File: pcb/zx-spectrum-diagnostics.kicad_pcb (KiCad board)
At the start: 2 copper layers, 99.9 x 98.2 mm, 75 parts, among them J101 Conn_01x04, J201 Conn_01x20_Female, J202 Conn_01x20_Female, J203 Conn_01x20_Female, Q101 PMBT2222A, SW101 SW_SPST, SW102 SW_SPST, U101 Pico, U102 Pico

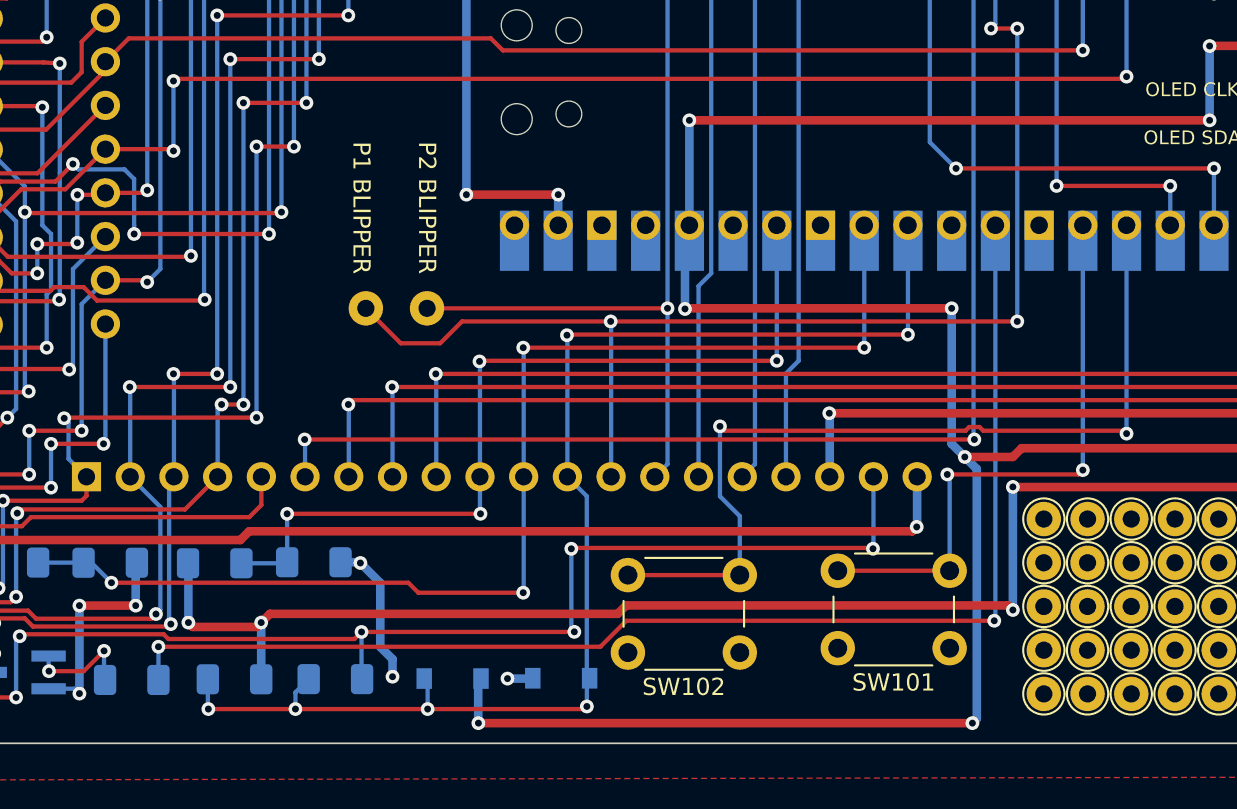
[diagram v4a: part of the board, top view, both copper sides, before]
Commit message: remove button2, reuse GPIO for ZXIORQ
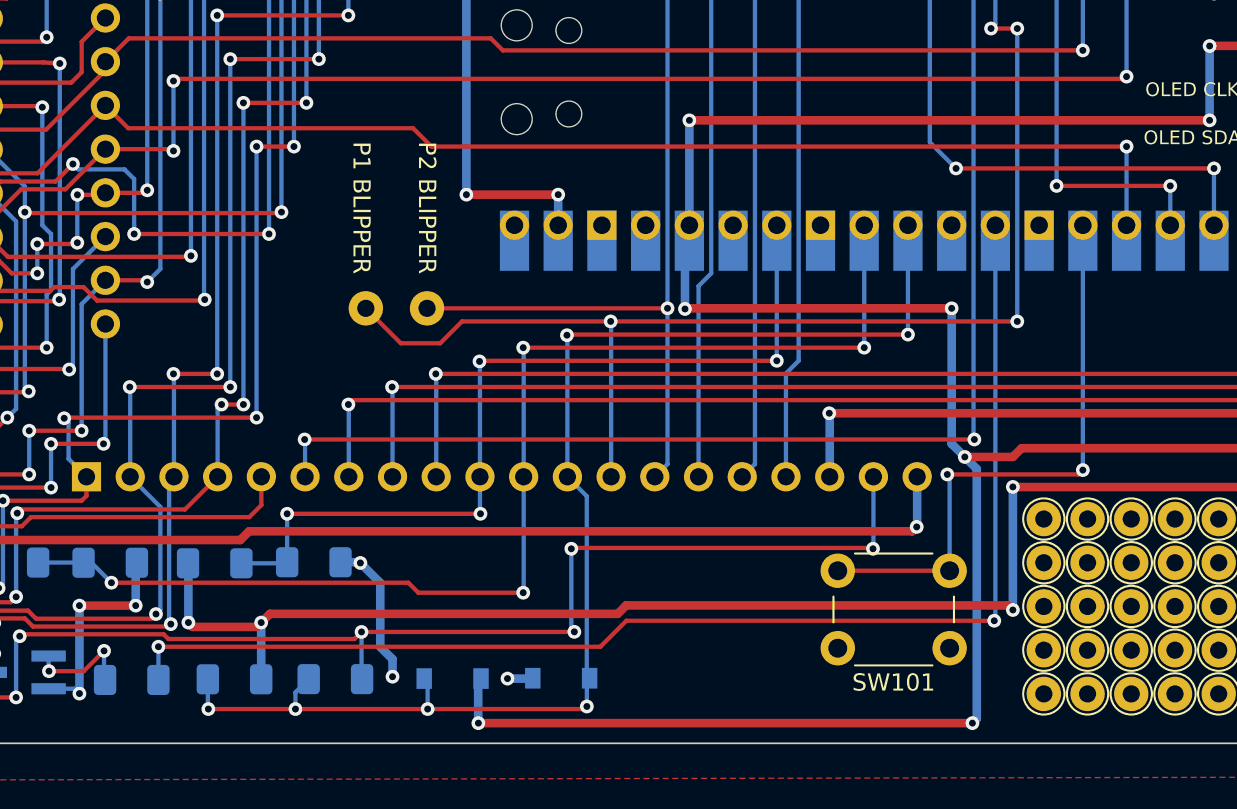
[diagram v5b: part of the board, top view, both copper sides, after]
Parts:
- removed SW102: SW_SPST, Button_Switch_THT:SW_PUSH_6mm_H4.3mm
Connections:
- U101 pad 26: INPUT2 -> ZXIORQ
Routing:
- net ZXIORQ: track 13.5 -> 78.4 mm, vias 0 -> 1
- net INPUT2: track 51.7 -> 0.00 mm, vias 2 -> 0
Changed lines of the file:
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@@
   (net 83 "PICO_RESET_Z80")
   (net 84 "INPUT1")
-  (net 85 "INPUT2")
-  (net 86 "unconnected-(Z101-PadA4)")
-  (net 87 "unconnected-(Z101-PadA28)")
+  (net 85 "unconnected-(Z101-PadA4)")
+  (net 86 "unconnected-(Z101-PadA28)")
   (footprint "TestPoint:TestPoint_THTPad_D2.0mm_Drill1.0mm" (layer "F.Cu")
     (at 166.69 148.64)
@@
       (net 61 "ZXD7") (pinfunction "D7") (pintype "input"))
     (pad "A4" thru_hole oval locked (at -25.4 -2.54 270) (size 1.7272 2.8) (drill 1.2) (layers *.Cu *.Mask)
-      (net 86 "unconnected-(Z101-PadA4)") (pinfunction "NC") (pintype "input+no_connect"))
+      (net 85 "unconnected-(Z101-PadA4)") (pinfunction "NC") (pintype "input+no_connect"))
     (pad "A6" thru_hole oval locked (at -20.32 -2.54 270) (size 1.7272 2.8) (drill 1.2) (layers *.Cu *.Mask)
       (net 62 "ZXD0") (pinfunction "D0") (pintype "input"))
@@
       (net 70 "ZXA10") (pinfunction "A10") (pintype "input"))
     (pad "A28" thru_hole oval locked (at 35.56 -2.54 270) (size 1.7272 2.8) (drill 1.2) (layers *.Cu *.Mask)
-      (net 87 "unconnected-(Z101-PadA28)") (pinfunction "NC") (pintype "input+no_connect"))
+      (net 86 "unconnected-(Z101-PadA28)") (pinfunction "NC") (pintype "input+no_connect"))
     (pad "B1" thru_hole oval locked (at -33.02 2.54 270) (size 1.7272 2.8) (drill 1.2) (layers *.Cu *.Mask)
       (net 58 "ZXA14") (pinfunction "A14") (pintype "input"))
@@
     (pad "1" thru_hole circle (at 0 0) (size 2 2) (drill 1) (layers *.Cu *.Mask))
   )
-  (footprint "Button_Switch_THT:SW_PUSH_6mm_H4.3mm" (layer "F.Cu")
-    (at 130.946 148.778 180)
-    (descr "tactile push button, 6x6mm e.g. PHAP33xx series, height=4.3mm")
-    (tags "tact sw push 6mm")
-    (property "Sheetfile" "zx-spectrum-diagnostics.kicad_sch")
-    (property "Sheetname" "")
-    (attr through_hole)
-    (fp_text reference "SW102" (at 3.25 -2) (layer "F.SilkS")
-      (effects (font (size 1 1) (thickness 0.15)))
-    )
-    (fp_text value "SW_SPST" (at 3.75 6.7) (layer "F.Fab")
-      (effects (font (size 1 1) (thickness 0.15)))
-    )
-    (fp_text user "${REFERENCE}" (at 3.25 2.25) (layer "F.Fab")
-      (effects (font (size 1 1) (thickness 0.15)))
-    )
-    (fp_line (start 5.5 -1) (end 1 -1) (layer "F.SilkS") (width 0.12))
-    (fp_line (start -0.25 1.5) (end -0.25 3) (layer "F.SilkS") (width 0.12))
-    (fp_line (start 1 5.5) (end 5.5 5.5) (layer "F.SilkS") (width 0.12))
-    (fp_line (start 6.75 3) (end 6.75 1.5) (layer "F.SilkS") (width 0.12))
-    (fp_line (start -1.5 5.75) (end -1.5 6) (layer "F.CrtYd") (width 0.05))
-    (fp_line (start 8 -1.25) (end 8 5.75) (layer "F.CrtYd") (width 0.05))
-    (fp_line (start -1.5 -1.25) (end -1.5 -1.5) (layer "F.CrtYd") (width 0.05))
-    (fp_line (start -1.5 6) (end -1.25 6) (layer "F.CrtYd") (width 0.05))
-    (fp_line (start 7.75 6) (end 8 6) (layer "F.CrtYd") (width 0.05))
-    (fp_line (start -1.5 -1.5) (end -1.25 -1.5) (layer "F.CrtYd") (width 0.05))
-    (fp_line (start 7.75 6) (end -1.25 6) (layer "F.CrtYd") (width 0.05))
-    (fp_line (start 8 -1.5) (end 8 -1.25) (layer "F.CrtYd") (width 0.05))
-    (fp_line (start 8 6) (end 8 5.75) (layer "F.CrtYd") (width 0.05))
-    (fp_line (start -1.5 5.75) (end -1.5 -1.25) (layer "F.CrtYd") (width 0.05))
-    (fp_line (start -1.25 -1.5) (end 7.75 -1.5) (layer "F.CrtYd") (width 0.05))
-    (fp_line (start 7.75 -1.5) (end 8 -1.5) (layer "F.CrtYd") (width 0.05))
-    (fp_line (start 6.25 5.25) (end 0.25 5.25) (layer "F.Fab") (width 0.1))
-    (fp_line (start 0.25 -0.75) (end 3.25 -0.75) (layer "F.Fab") (width 0.1))
-    (fp_line (start 0.25 5.25) (end 0.25 -0.75) (layer "F.Fab") (width 0.1))
-    (fp_line (start 3.25 -0.75) (end 6.25 -0.75) (layer "F.Fab") (width 0.1))
-    (fp_line (start 6.25 -0.75) (end 6.25 5.25) (layer "F.Fab") (width 0.1))
-    (fp_circle (center 3.25 2.25) (end 1.25 2.5) (layer "F.Fab") (width 0.1) (fill none))
-    (pad "1" thru_hole circle (at 0 0 270) (size 2 2) (drill 1.1) (layers *.Cu *.Mask)
-      (net 5 "GND") (pinfunction "A") (pintype "passive"))
-    (pad "1" thru_hole circle (at 6.5 0 270) (size 2 2) (drill 1.1) (layers *.Cu *.Mask)
-      (net 5 "GND") (pinfunction "A") (pintype "passive"))
-    (pad "2" thru_hole circle (at 0 4.5 270) (size 2 2) (drill 1.1) (layers *.Cu *.Mask)
-      (net 85 "INPUT2") (pinfunction "B") (pintype "passive"))
-    (pad "2" thru_hole circle (at 6.5 4.5 270) (size 2 2) (drill 1.1) (layers *.Cu *.Mask)
-      (net 85 "INPUT2") (pinfunction "B") (pintype "passive"))
-    (model "${KICAD6_3DMODEL_DIR}/Button_Switch_THT.3dshapes/SW_PUSH_6mm_H4.3mm.wrl"
-      (offset (xyz 0 0 0))
-      (scale (xyz 1 1 1))
-      (rotate (xyz 0 0 0))
-    )
-  )
   (footprint "TestPoint:TestPoint_THTPad_D2.0mm_Drill1.0mm" (layer "F.Cu")
     (at 164.15 141.02)
@@
       (net 13 "P2_LINKIN") (pinfunction "GPIO19") (pintype "bidirectional"))
     (pad "26" thru_hole oval (at 8.89 -11.43 270) (size 1.7 1.7) (drill 1.02) (layers *.Cu *.Mask)
-      (net 85 "INPUT2") (pinfunction "GPIO20") (pintype "bidirectional"))
+      (net 78 "ZXIORQ") (pinfunction "GPIO20") (pintype "bidirectional"))
     (pad "26" smd rect (at 8.89 -11.43 270) (size 3.5 1.7) (drill (offset 0.9 0)) (layers "B.Cu" "B.Mask")
-      (net 85 "INPUT2") (pinfunction "GPIO20") (pintype "bidirectional"))
+      (net 78 "ZXIORQ") (pinfunction "GPIO20") (pintype "bidirectional"))
     (pad "27" thru_hole oval (at 8.89 -8.89 270) (size 1.7 1.7) (drill 1.02) (layers *.Cu *.Mask)
       (net 84 "INPUT1") (pinfunction "GPIO21") (pintype "bidirectional"))
@@
   (gr_line (start 141.158 150.338) (end 141.92 149.576) (layer "B.SilkS") (width 0.15))
   (gr_rect (start 143.088 136.981) (end 135.128 140.462) (layer "B.SilkS") (width 0.15) (fill solid))
-  (gr_line (start 128.966 150.338) (end 129.728 149.83) (layer "B.SilkS") (width 0.15))
-  (gr_line (start 126.426 150.592) (end 125.664 149.83) (layer "B.SilkS") (width 0.15))
   (gr_line (start 138.872 150.338) (end 137.856 149.576) (layer "B.SilkS") (width 0.15))
   (gr_rect (start 76.2 90.678) (end 84.396 92.68) (layer "F.SilkS") (width 0.15) (fill solid))
@@
     (effects (font (size 0.8 0.8) (thickness 0.125)) (justify right mirror))
   )
-  (gr_text "GNDs" (at 127.696 150.846) (layer "B.SilkS")
-    (effects (font (size 0.5 0.5) (thickness 0.125)) (justify mirror))
-  )
   (gr_text "P1\nBLIP" (at 123.444 141.224) (layer "B.SilkS")
     (effects (font (size 0.8 0.8) (thickness 0.125)) (justify mirror))
@@
   (segment (start 153.416 115.316) (end 153.416 106.172) (width 0.25) (layer "B.Cu") (net 77))
   (segment (start 98.044 119.634) (end 98.044 115.57) (width 0.25) (layer "B.Cu") (net 77))
+  (segment (start 113.03 119.38) (end 153.416 119.38) (width 0.25) (layer "F.Cu") (net 78))
   (segment (start 85.374 122.144) (end 82.738 122.144) (width 0.25) (layer "F.Cu") (net 78))
   (segment (start 94.09 116.99) (end 90.145 120.935) (width 0.25) (layer "F.Cu") (net 78))
+  (segment (start 111.965123 118.315123) (end 113.03 119.38) (width 0.25) (layer "F.Cu") (net 78))
   (segment (start 86.583 120.935) (end 85.374 122.144) (width 0.25) (layer "F.Cu") (net 78))
+  (segment (start 95.415123 118.315123) (end 111.965123 118.315123) (width 0.25) (layer "F.Cu") (net 78))
   (segment (start 90.145 120.935) (end 86.583 120.935) (width 0.25) (layer "F.Cu") (net 78))
+  (segment (start 94.09 116.99) (end 95.415123 118.315123) (width 0.25) (layer "F.Cu") (net 78))
+  (via (at 153.416 119.38) (size 0.8) (drill 0.4) (layers "F.Cu" "B.Cu") (net 78))
+  (segment (start 153.416 119.38) (end 153.416 123.952) (width 0.25) (layer "B.Cu") (net 78))
   (segment (start 94.09 114.952) (end 90.647 118.395) (width 0.25) (layer "F.Cu") (net 79))
   (segment (start 95.445 113.095) (end 116.481122 113.095) (width 0.25) (layer "F.Cu") (net 79))
@@
   (segment (start 143.138 138.566) (end 143.002 138.43) (width 0.25) (layer "B.Cu") (net 84))
   (segment (start 143.138 144.024) (end 143.138 138.566) (width 0.25) (layer "B.Cu") (net 84))
-  (segment (start 144.873702 135.673) (end 144.273092 135.673) (width 0.25) (layer "F.Cu") (net 85))
-  (segment (start 130.048 135.89) (end 129.794 135.636) (width 0.25) (layer "F.Cu") (net 85))
-  (segment (start 145.090702 135.89) (end 144.873702 135.673) (width 0.25) (layer "F.Cu") (net 85))
-  (segment (start 153.416 136.0565) (end 153.2495 135.89) (width 0.25) (layer "F.Cu") (net 85))
-  (segment (start 153.2495 135.89) (end 145.090702 135.89) (width 0.25) (layer "F.Cu") (net 85))
-  (segment (start 144.273092 135.673) (end 144.056092 135.89) (width 0.25) (layer "F.Cu") (net 85))
-  (segment (start 144.056092 135.89) (end 130.048 135.89) (width 0.25) (layer "F.Cu") (net 85))
-  (segment (start 124.446 144.278) (end 130.946 144.278) (width 0.25) (layer "F.Cu") (net 85))
-  (via (at 153.416 136.0565) (size 0.8) (drill 0.4) (layers "F.Cu" "B.Cu") (net 85))
-  (via (at 129.794 135.636) (size 0.8) (drill 0.4) (layers "F.Cu" "B.Cu") (net 85))
-  (segment (start 153.416 136.0565) (end 153.416 123.952) (width 0.25) (layer "B.Cu") (net 85))
-  (segment (start 130.946 140.852) (end 129.794 139.7) (width 0.25) (layer "B.Cu") (net 85))
-  (segment (start 129.794 139.7) (end 129.794 135.636) (width 0.25) (layer "B.Cu") (net 85))
-  (segment (start 130.946 144.278) (end 130.946 140.852) (width 0.25) (layer "B.Cu") (net 85))
   (zone (net 5) (net_name "GND") (layer "F.Cu") (hatch edge 0.508)
     (connect_pads (clearance 0.508))

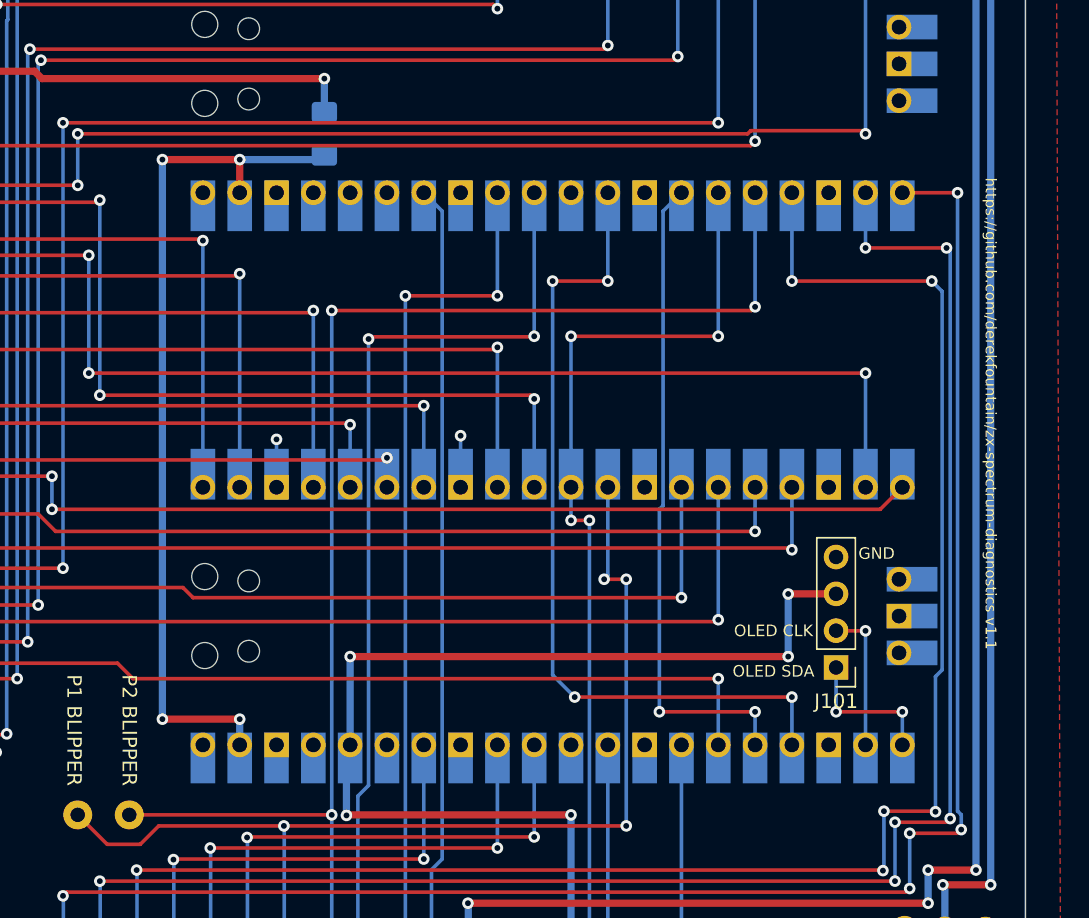
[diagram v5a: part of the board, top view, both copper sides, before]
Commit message: have a required test value sent over to pico2 at the start. add test code to fill the address buffer. works but shows the odd restarting effect i saw when i was doing the ROM emulator
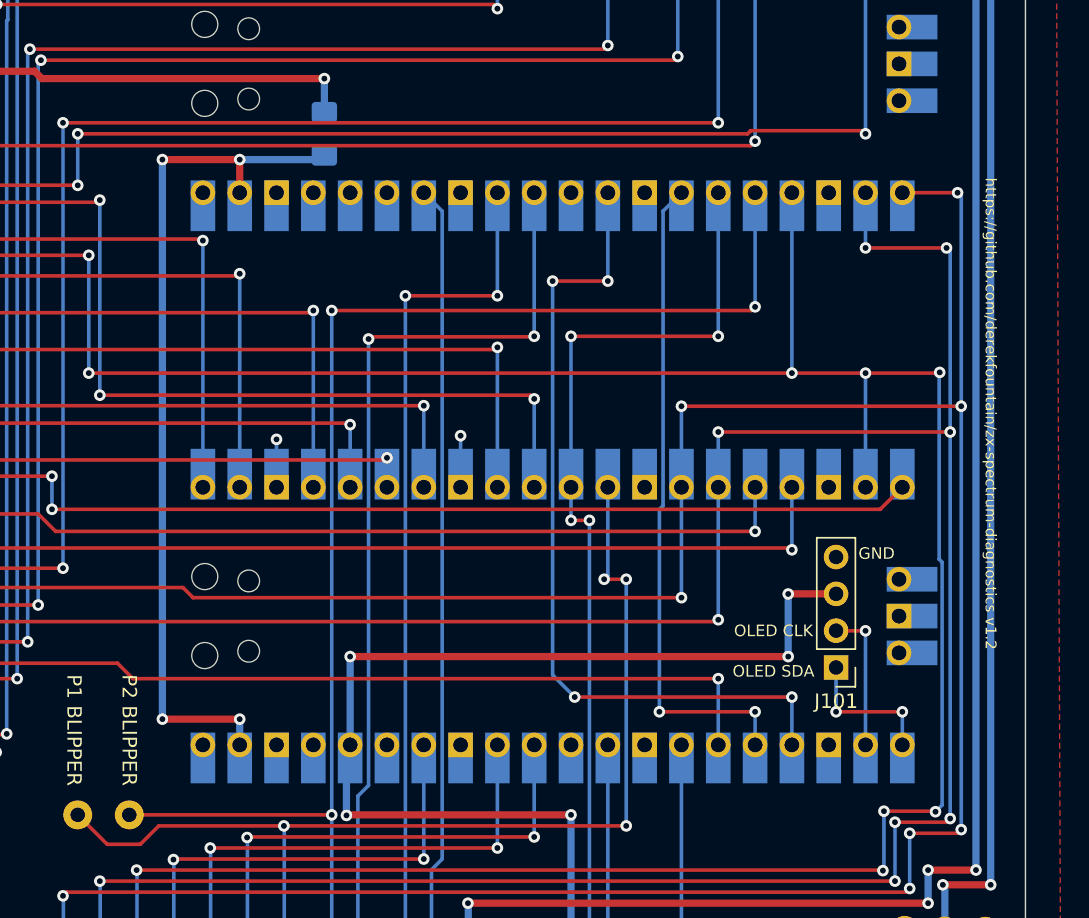
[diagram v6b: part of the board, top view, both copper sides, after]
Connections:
- J202 pad 7: P2_GPIO16 -> ZXMREQ
- J202 pad 8: P2_GPIO17 -> ZXRD
- J202 pad 9: P2_GPIO18 -> ZXCLK
- U102 pad 21: P2_GPIO16 -> ZXMREQ
- U102 pad 22: P2_GPIO17 -> ZXRD
- U102 pad 24: P2_GPIO18 -> ZXCLK
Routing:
- net ZXMREQ: track 78.6 -> 221.6 mm, vias 1 -> 8
- net ZXRD: track 86.2 -> 223.0 mm, vias 3 -> 11
- net P2_GPIO16: track 118.2 -> 0.00 mm, vias 5 -> 0
- net P2_GPIO18: track 118.0 -> 0.00 mm, vias 6 -> 0
- net P2_GPIO17: track 116.9 -> 0.00 mm, vias 6 -> 0
- net ZXCLK: track 112.5 -> 225.9 mm, vias 7 -> 13
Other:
- board text added: "https://github.com/derekfountain/zx-spectrum-diagnostics v1.2"
- board text removed: "https://github.com/derekfountain/zx-spectrum-diagnostics v1.1"

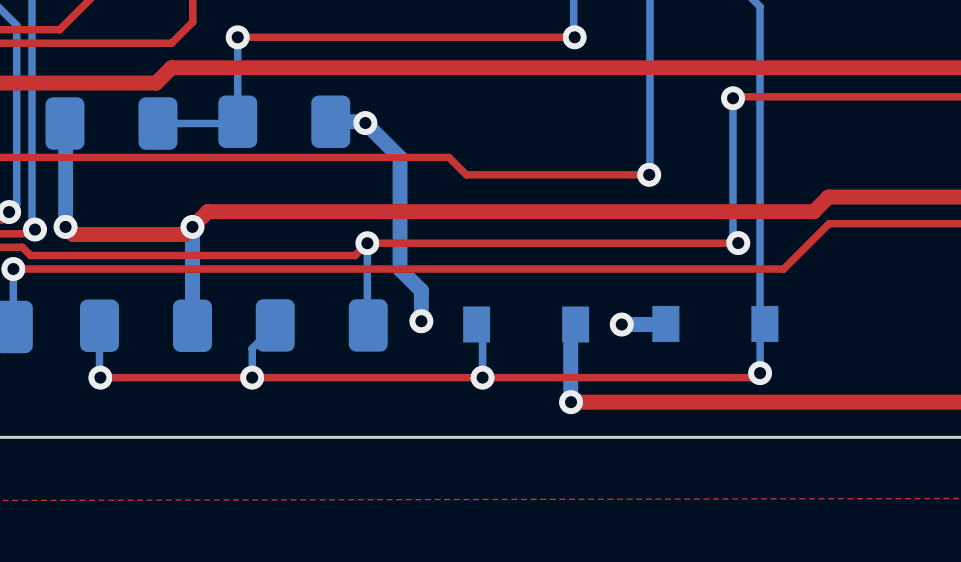
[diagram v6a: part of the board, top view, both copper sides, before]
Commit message: update schematic and PCB with revised -5V voltage divider
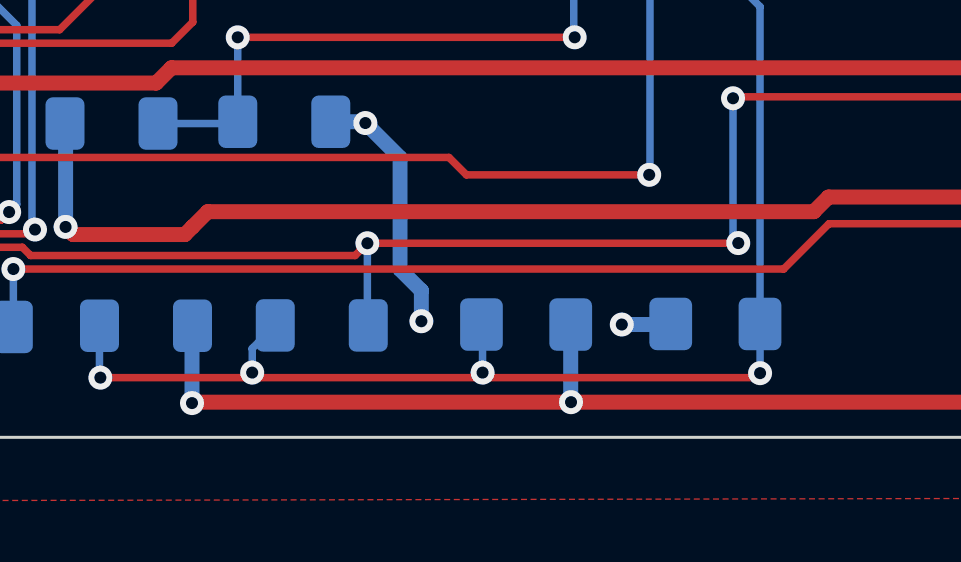
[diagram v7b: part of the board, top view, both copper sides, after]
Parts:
- D102, D103: value 1N4148 -> D_Schottky; footprint Diode_SMD:D_SOD-123 -> Diode_SMD:D_1206_3216Metric_Pad1.42x1.75mm_HandSolder
- R101: value 1K5 -> 390R
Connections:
- R101 pad 1: +5V -> 3V3_PICO1
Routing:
- net 3V3_PICO1: track 142.6 -> 157.8 mm, vias 8 -> 9
- net +5V: track 345.8 -> 342.5 mm, vias 10 -> 9
